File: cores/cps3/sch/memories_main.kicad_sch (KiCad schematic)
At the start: 8 parts

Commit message: main_obj
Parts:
- removed KA10, KA12, KA13, KA14, KB10, KB12, KB13, KB14: 29F016-90PFTN, symbol arcade:29F016-90PFTN
- added 2D, 3D, 4D, 5D: HM5118160AJ, symbol oki:HM5118160AJ
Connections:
- net VCC: now also 2D.1 (VCC), 2D.21 (VCC), 2D.6 (VCC), 3D.1 (VCC), 3D.21 (VCC), 3D.6 (VCC), 4D.1 (VCC), 4D.21 (VCC), 4D.6 (VCC), 5D.1 (VCC), 5D.21 (VCC), 5D.6 (VCC)
- net VSS: now also 2D.22 (VSS), 2D.37 (VSS), 2D.42 (VSS), 3D.22 (VSS), 3D.37 (VSS), 3D.42 (VSS), 4D.22 (VSS), 4D.37 (VSS), 4D.42 (VSS), 5D.22 (VSS), 5D.37 (VSS), 5D.42 (VSS)
- new net OE_A: 2D.29 (~{OE}), 4D.29 (~{OE})
- new net OE_B: 3D.29 (~{OE}), 5D.29 (~{OE})
- new net PPU_A0: 2D.17 (A0), 3D.17 (A0), 4D.17 (A0), 5D.17 (A0)
- new net PPU_A1: 2D.18 (A1), 3D.18 (A1), 4D.18 (A1), 5D.18 (A1)
- new net PPU_A2: 2D.19 (A2), 3D.19 (A2), 4D.19 (A2), 5D.19 (A2)
- new net PPU_A3: 2D.20 (A3), 3D.20 (A3), 4D.20 (A3), 5D.20 (A3)
- new net PPU_A4: 2D.23 (A4), 3D.23 (A4), 4D.23 (A4), 5D.23 (A4)
- new net PPU_A5: 2D.24 (A5), 3D.24 (A5), 4D.24 (A5), 5D.24 (A5)
- new net PPU_A6: 2D.25 (A6), 3D.25 (A6), 4D.25 (A6), 5D.25 (A6)
- new net PPU_A7: 2D.26 (A7), 3D.26 (A7), 4D.26 (A7), 5D.26 (A7)
- new net PPU_A8: 2D.27 (A8), 3D.27 (A8), 4D.27 (A8), 5D.27 (A8)
- new net PPU_A9: 2D.28 (A9), 3D.28 (A9), 4D.28 (A9), 5D.28 (A9)
- new net PPU_D0: 2D.2 (D0), 3D.2 (D0)
- new net PPU_D1: 2D.3 (D1), 3D.3 (D1)
- new net PPU_D10: 2D.35 (D10), 3D.35 (D10)
- new net PPU_D11: 2D.36 (D11), 3D.36 (D11)
- new net PPU_D12: 2D.38 (D12), 3D.38 (D12)
- new net PPU_D13: 2D.39 (D13), 3D.39 (D13)
- new net PPU_D14: 2D.40 (D14), 3D.40 (D14)
- new net PPU_D15: 2D.41 (D15), 3D.41 (D15)
- new net PPU_D16: 4D.2 (D0), 5D.2 (D0)
- new net PPU_D17: 4D.3 (D1), 5D.3 (D1)
- new net PPU_D18: 4D.4 (D2), 5D.4 (D2)
- new net PPU_D19: 4D.5 (D3), 5D.5 (D3)
- new net PPU_D2: 2D.4 (D2), 3D.4 (D2)
- new net PPU_D20: 4D.7 (D4), 5D.7 (D4)
- new net PPU_D21: 4D.8 (D5), 5D.8 (D5)
- new net PPU_D22: 4D.9 (D6), 5D.9 (D6)
- new net PPU_D23: 4D.10 (D7), 5D.10 (D7)
- new net PPU_D24: 4D.33 (D8), 5D.33 (D8)
- new net PPU_D25: 4D.34 (D9), 5D.34 (D9)
- new net PPU_D26: 4D.35 (D10), 5D.35 (D10)
- new net PPU_D27: 4D.36 (D11), 5D.36 (D11)
- new net PPU_D28: 4D.38 (D12), 5D.38 (D12)
- new net PPU_D29: 4D.39 (D13), 5D.39 (D13)
- new net PPU_D3: 2D.5 (D3), 3D.5 (D3)
- new net PPU_D30: 4D.40 (D14), 5D.40 (D14)
- new net PPU_D31: 4D.41 (D15), 5D.41 (D15)
- new net PPU_D4: 2D.7 (D4), 3D.7 (D4)
- new net PPU_D5: 2D.8 (D5), 3D.8 (D5)
- new net PPU_D6: 2D.9 (D6), 3D.9 (D6)
- new net PPU_D7: 2D.10 (D7), 3D.10 (D7)
- new net PPU_D8: 2D.33 (D8), 3D.33 (D8)
- new net PPU_D9: 2D.34 (D9), 3D.34 (D9)
- new net ~{LCAS}_A: 2D.31 (~{LCAS})
- new net ~{LCAS}_B: 3D.31 (~{LCAS})
- new net ~{LCAS}_C: 4D.31 (~{LCAS})
- new net ~{LCAS}_D: 5D.31 (~{LCAS})
- new net ~{RAS}: 2D.14 (~{RAS}), 3D.14 (~{RAS}), 4D.14 (~{RAS}), 5D.14 (~{RAS})
- new net ~{UCAS}_A: 2D.30 (~{UCAS})
- new net ~{UCAS}_B: 3D.30 (~{UCAS})
- new net ~{UCAS}_C: 4D.30 (~{UCAS})
- new net ~{UCAS}_D: 5D.30 (~{UCAS})
- new net ~{WE}_A: 2D.13 (~{WE}), 4D.13 (~{WE})
- new net ~{WE}_B: 3D.13 (~{WE}), 5D.13 (~{WE})
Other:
- note added: "MEMORIES MAIN?"
- note removed: "The pattern table"

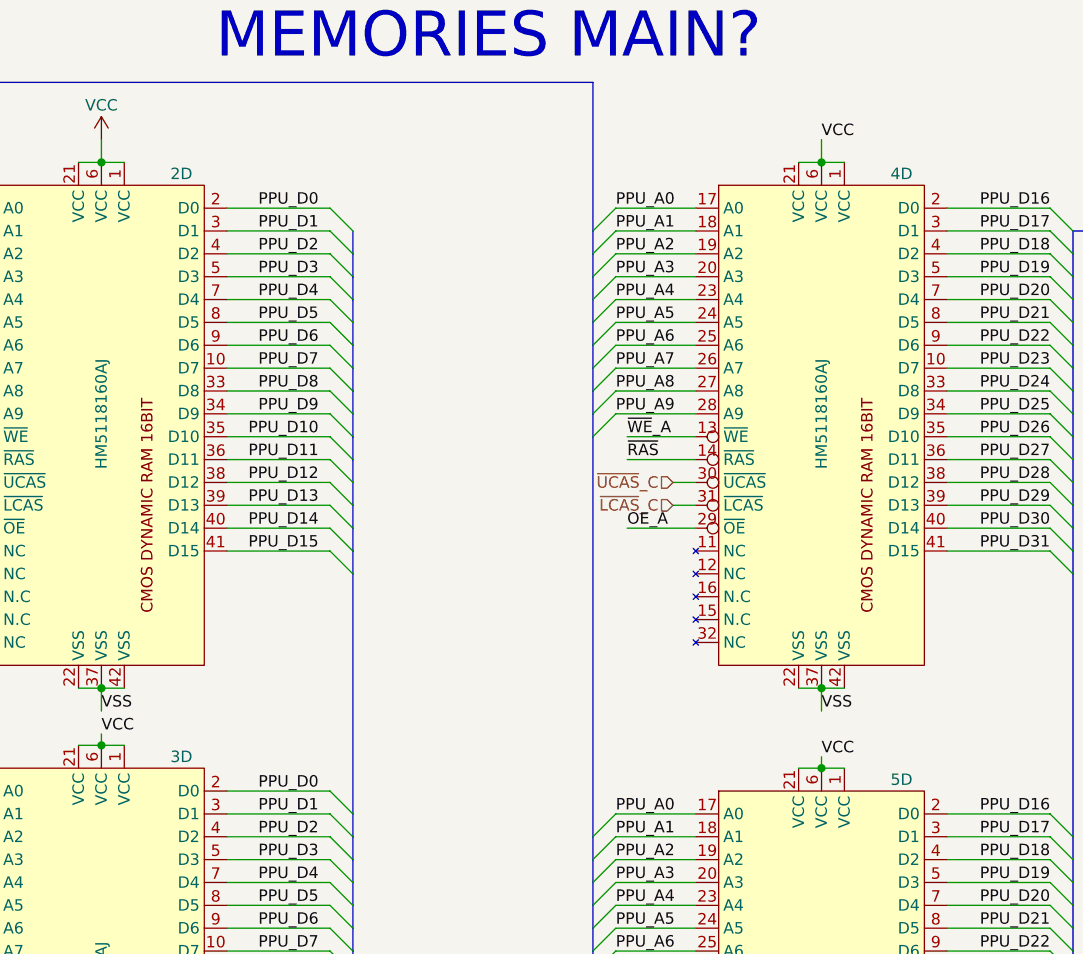
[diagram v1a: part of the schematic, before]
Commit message: new_symbols
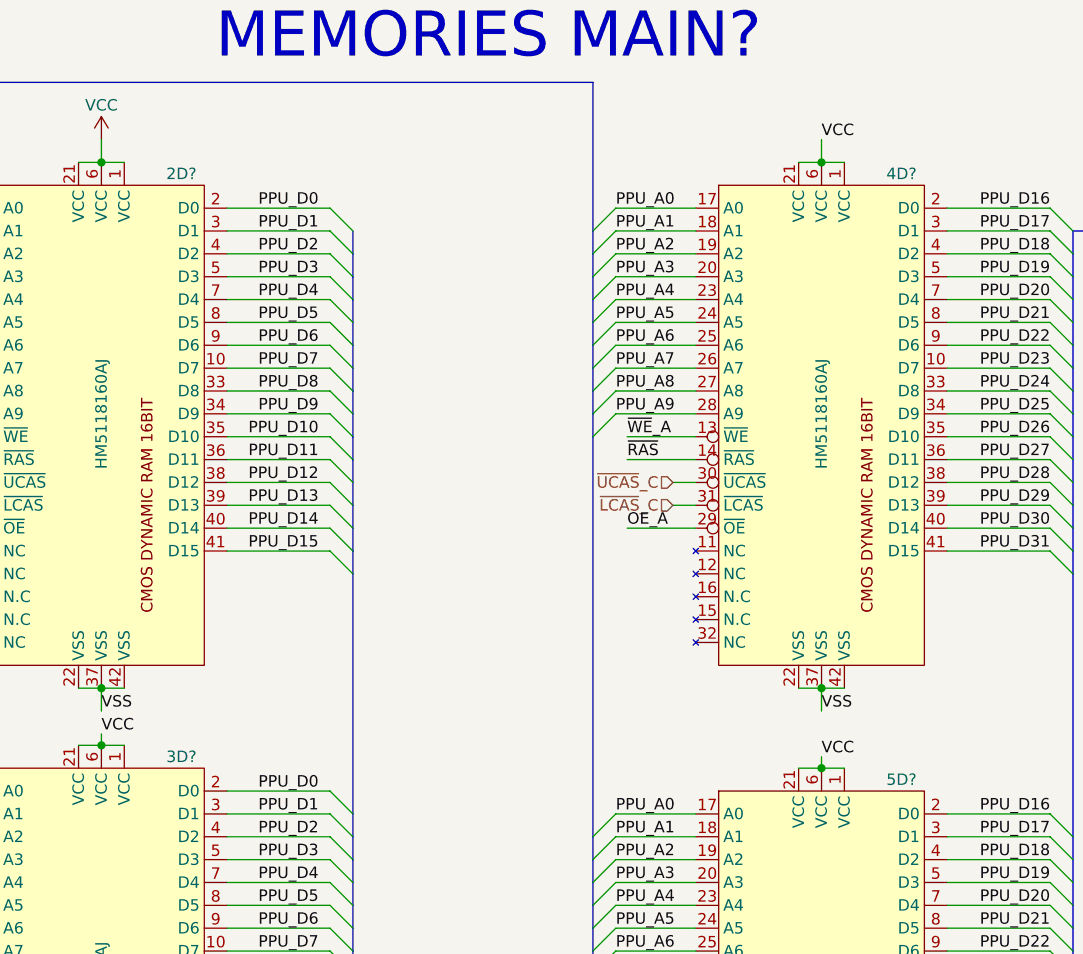
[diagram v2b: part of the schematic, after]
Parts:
- renumbered 2D to 2D?, 3D to 3D?, 4D to 4D?, 5D to 5D?
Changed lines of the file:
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@@
   (symbol (lib_name "HM5118160AJ_3") (lib_id "oki:HM5118160AJ") (at 74.93 123.19 0) (unit 1)
     (in_bom yes) (on_board yes)
-    (property "Reference" "3D" (id 0) (at 83.82 96.52 0))
+    (property "Reference" "3D?" (id 0) (at 83.82 96.52 0))
     (property "Value" "HM5118160AJ" (id 1) (at 74.93 123.19 90))
     (property "Footprint" "" (id 2) (at 74.93 123.19 0)
@@
   (symbol (lib_id "oki:HM5118160AJ") (at 154.94 125.73 0) (unit 1)
     (in_bom yes) (on_board yes)
-    (property "Reference" "5D" (id 0) (at 163.83 99.06 0))
+    (property "Reference" "5D?" (id 0) (at 163.83 99.06 0))
     (property "Value" "HM5118160AJ" (id 1) (at 154.94 125.73 90))
     (property "Footprint" "" (id 2) (at 154.94 125.73 0)
@@
   (symbol (lib_name "HM5118160AJ_1") (lib_id "oki:HM5118160AJ") (at 74.93 58.42 0) (unit 1)
     (in_bom yes) (on_board yes)
-    (property "Reference" "2D" (id 0) (at 83.82 31.75 0))
+    (property "Reference" "2D?" (id 0) (at 83.82 31.75 0))
     (property "Value" "HM5118160AJ" (id 1) (at 74.93 58.42 90))
     (property "Footprint" "" (id 2) (at 74.93 58.42 0)
@@
   (symbol (lib_name "HM5118160AJ_2") (lib_id "oki:HM5118160AJ") (at 154.94 58.42 0) (unit 1)
     (in_bom yes) (on_board yes)
-    (property "Reference" "4D" (id 0) (at 163.83 31.75 0))
+    (property "Reference" "4D?" (id 0) (at 163.83 31.75 0))
     (property "Value" "HM5118160AJ" (id 1) (at 154.94 58.42 90))
     (property "Footprint" "" (id 2) (at 154.94 58.42 0)

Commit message: ssu_gll
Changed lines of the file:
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@@
     (effects (font (size 1.27 1.27)) (justify right))
   )
-  (hierarchical_label "PPU_D[0..31]" (shape output) (at 190.5 38.1 0)
+  (hierarchical_label "PPU_D[31..0]" (shape output) (at 190.5 38.1 0)
     (effects (font (size 1.27 1.27)) (justify left))
   )

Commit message: update_cps3
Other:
- note added: "MEMORIES FRAME BUFFER?"
- note removed: "MEMORIES MAIN?"
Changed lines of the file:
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@@
     )
   )
-  (text "MEMORIES MAIN?\n\n\n" (at 87.63 35.56 0)
+  (text "MEMORIES FRAME BUFFER?\n\n\n" (at 87.63 35.56 0)
     (effects (font (size 5 5)) (justify left bottom))
   )
